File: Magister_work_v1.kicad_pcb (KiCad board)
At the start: 4 copper layers, 80 x 80 mm, 170 parts, among them J1 USB_B_Mini, J15 Conn_01x02_Pin, J17 Conn_01x04_Pin, J2 Conn_01x03_Pin, J3 Conn_01x03_Pin, J6 Conn_01x04_Pin, J7 Conn_01x02_Pin, J8 Conn_01x06_Pin, J9 Conn_01x02_Pin, Q1 AO3400A, Q10 PDTC143ET, Q11 PDTC143ET, Q12 PDTC143ET, Q2 AO3400A, Q3 PDTC143ET, Q4 PDTC143ET, Q5 PDTC143ET, Q6 PDTC143ET, Q7 PDTC143ET, Q8 PDTC143ET, Q9 PDTC143ET, SW1 SW_Push, SW10 SW_Push, SW11 SW_Push, SW12 SW_Push, SW2 SW_Push, SW3 SW_Push, SW4 SW_Push, SW5 SW_Push, SW6 SW_Push, SW7 SW_Push, SW8 SW_Push, SW9 SW_Push, U10 SRV05-4, U3 Ai-Thinker-Ra-01, U5 AMS1117-3.3, U7 STM32F407VETx, U8 AT24C256, U9 Ai-Thinker-Ra-01SH, Y1 X322525MQB4SI, Y2 SMD03215C2

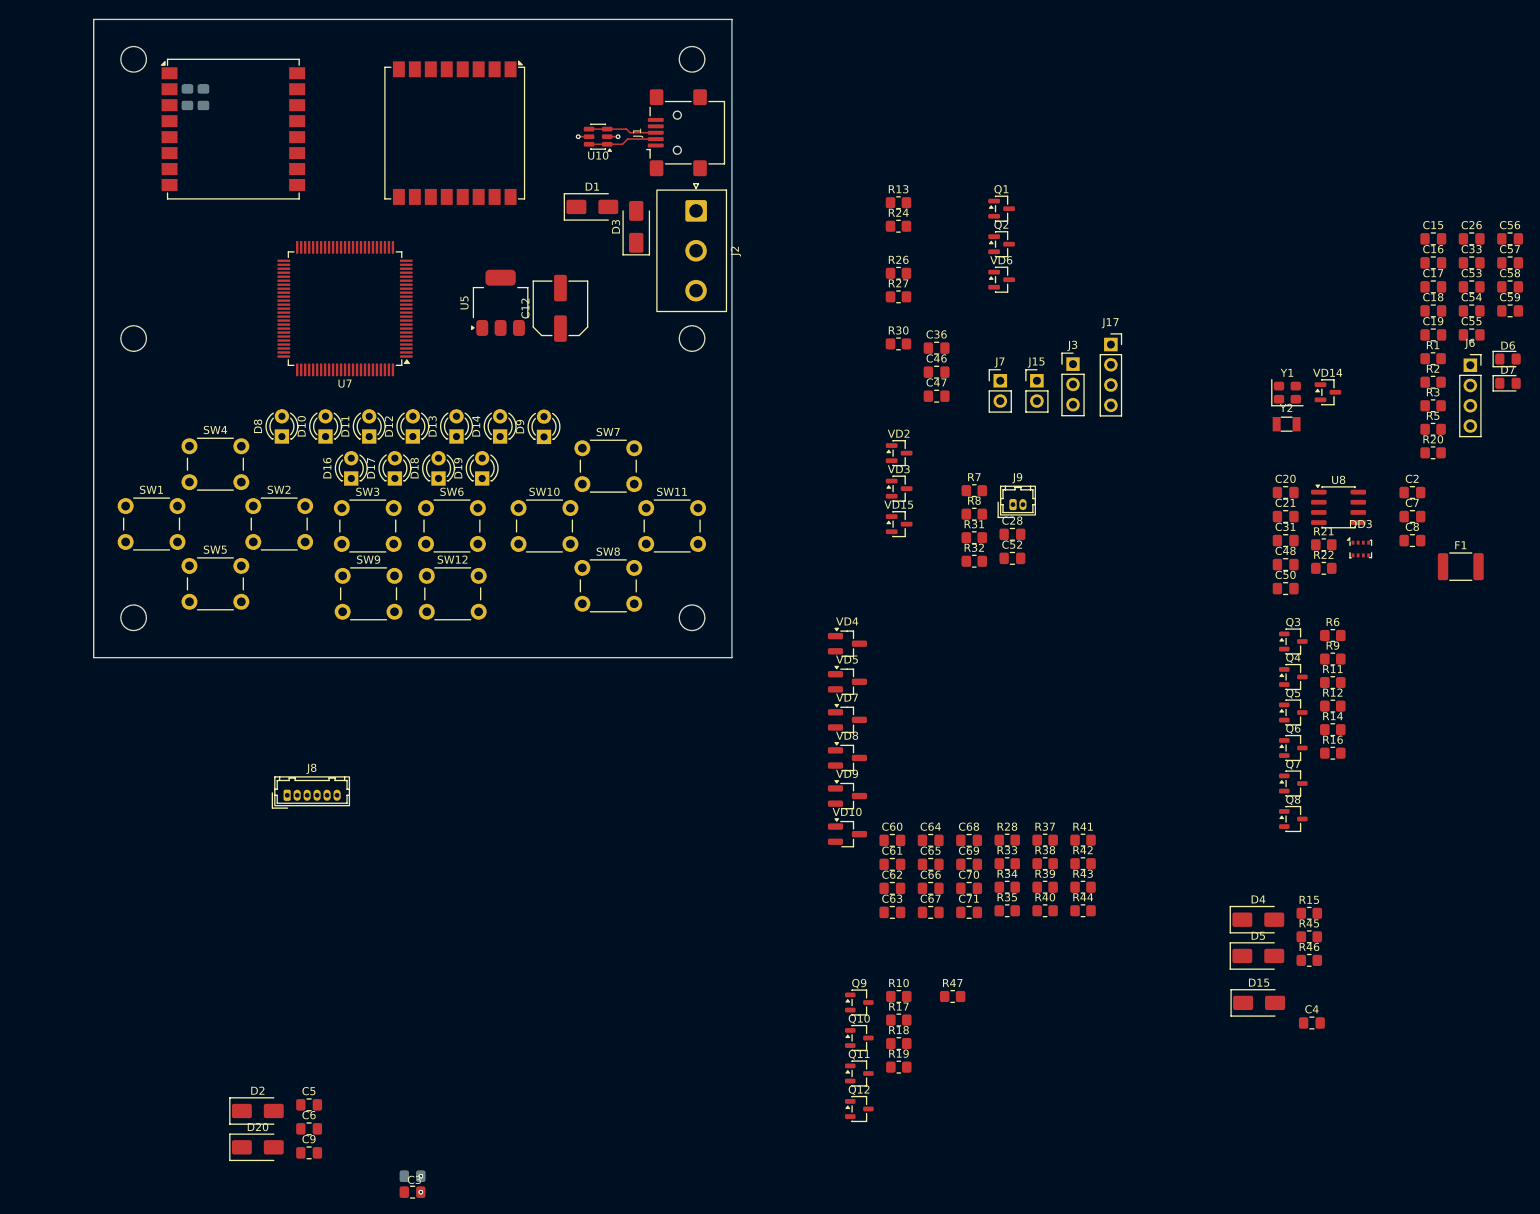
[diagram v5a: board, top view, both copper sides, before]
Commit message: feat: расположены основные узлы модуля на печатной плате
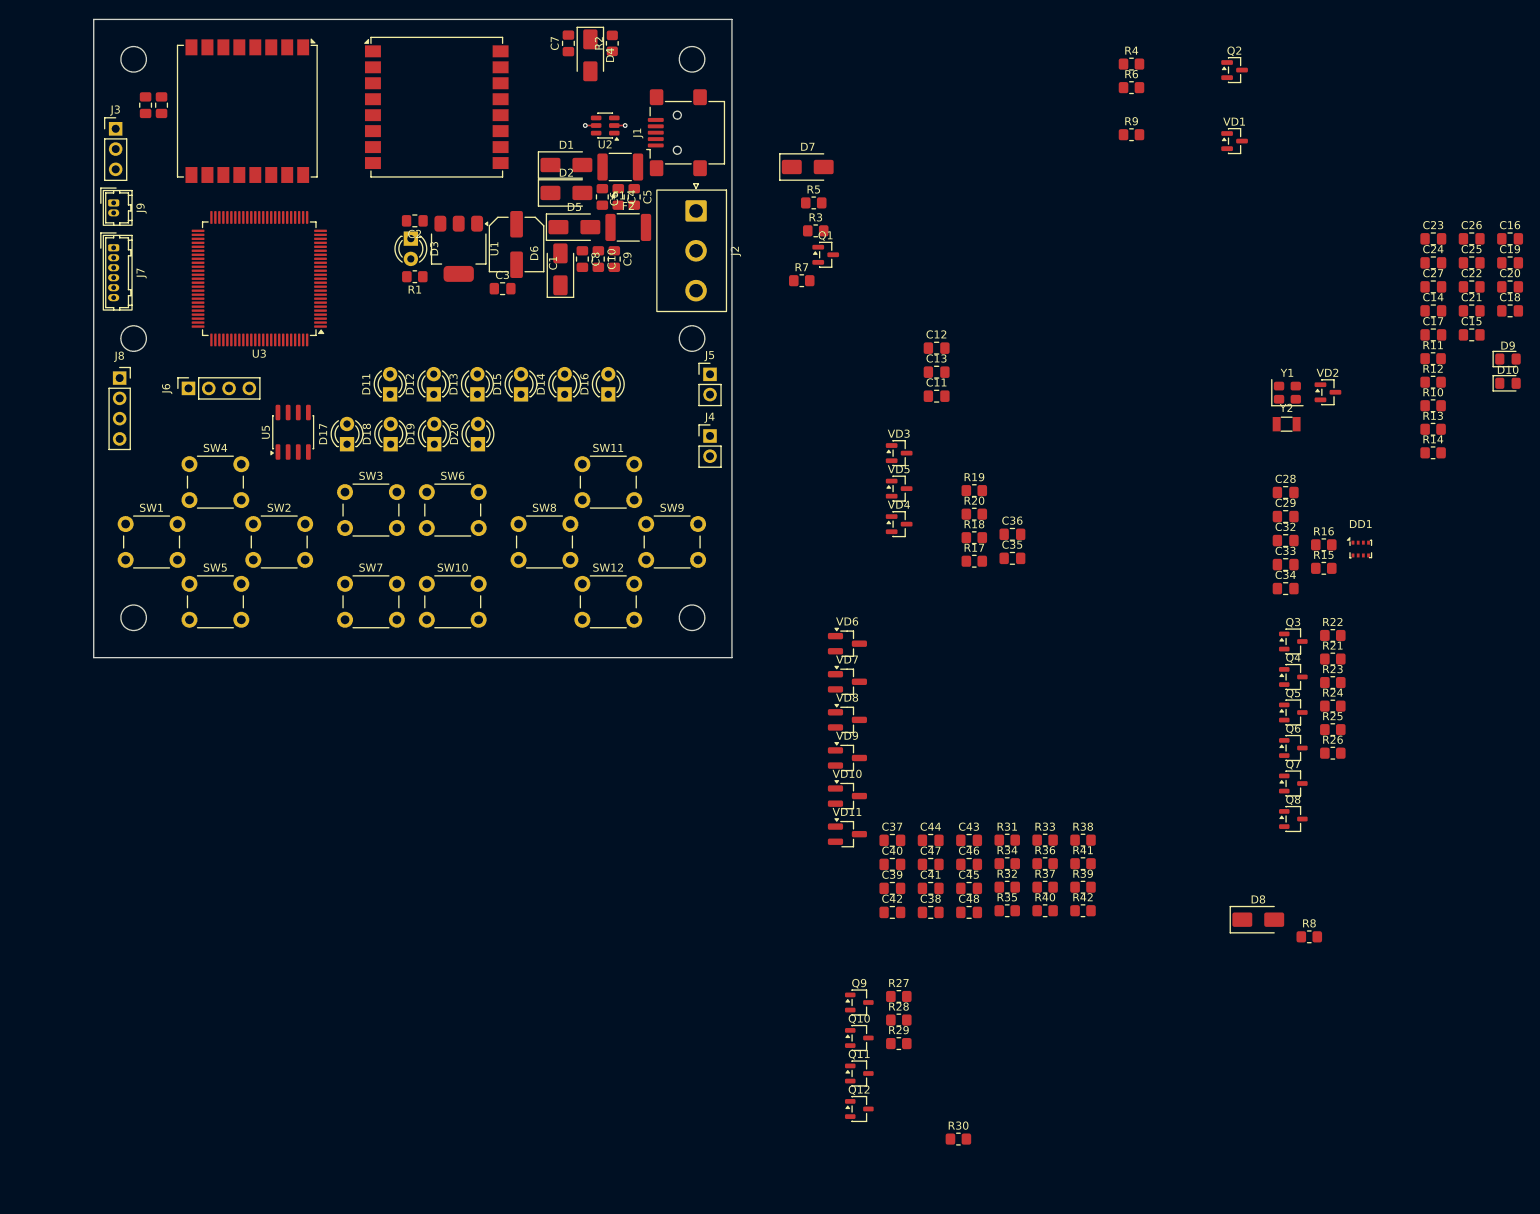
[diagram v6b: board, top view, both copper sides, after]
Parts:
- added F2: MF-MSMF110-2, Fuse:Fuse_1812_4532Metric_Pad1.30x3.40mm_HandSolder, F.Cu at (97.0, 56.1)
- C30: renamed from C32; moved to F.Cu
- C31: renamed from C49; moved to F.Cu
- C4: renamed from C1; moved to F.Cu
- moved J6 160.7 mm to (41.9, 76.2), turned to 90 degrees
- moved C7 154.2 mm to (89.5, 33.0), turned to 90 degrees
- moved D4 145.4 mm to (92.2, 34.5), turned to -90 degrees
- moved R2 139.7 mm to (95.0, 33.0), turned to 90 degrees
- moved U5 131.4 mm to (55.0, 81.8), turned to 90 degrees
- moved C2 130.4 mm to (70.2, 55.2), turned to 180 degrees
- moved C6 127.0 mm to (93.8, 52.2), turned to -90 degrees
- moved C4 125.4 mm to (95.8, 52.2), turned to -90 degrees
- moved J8 124.3 mm to (33.2, 75.0)
- moved J3 123.6 mm to (32.8, 43.7)
- moved J9 118.9 mm to (32.5, 53.0), turned to -90 degrees
- moved C3 118.3 mm to (81.2, 63.8)
- moved C10 117.8 mm to (93.2, 60.0), turned to -90 degrees
- moved D5 117.7 mm to (90.2, 56.0)
- moved F1 116.7 mm to (96.0, 48.5), turned to 180 degrees
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- renumbered C12 to C1, C9 to C10, C47 to C11, C36 to C12, C46 to C13, C18 to C14, C55 to C15, C56 to C16, C19 to C17, C59 to C18, C57 to C19, C7 to C2, C58 to C20, C54 to C21, C53 to C22, C15 to C23, C16 to C24, C33 to C25, C17 to C27, C20 to C28, C21 to C29, C8 to C3, C31 to C32, C48 to C33, C50 to C34, C52 to C35, C28 to C36, C60 to C37, C67 to C38, C62 to C39, C61 to C40, C66 to C41, C63 to C42, C68 to C43, C64 to C44, C70 to C45, C69 to C46, C65 to C47, C71 to C48, C2 to C5, C3 to C6, C4 to C7, C5 to C8, C6 to C9, D7 to D10, D8 to D11, D10 to D12, D11 to D13, D13 to D14, D12 to D15, D14 to D16, D16 to D17, D17 to D18, D18 to D19, D3 to D2, D19 to D20, D9 to D3, D15 to D4, D2 to D5, D20 to D6, D5 to D7, D4 to D8, D6 to D9, DD3 to DD1, J15 to J4, J7 to J5, J8 to J7, J17 to J8, Q2 to Q1, Q1 to Q2, R47 to R1, R3 to R10, R1 to R11, R2 to R12, R5 to R13, R20 to R14, R22 to R15, R21 to R16, R32 to R17, R31 to R18, R7 to R19, R15 to R2, R8 to R20, R9 to R21, R6 to R22, R11 to R23, R12 to R24, R14 to R25, R16 to R26, R10 to R27, R17 to R28, R18 to R29, R27 to R3, R19 to R30, R28 to R31, R34 to R32, R37 to R33, R33 to R34, R38 to R36, R39 to R37, R41 to R38, R43 to R39, R13 to R4, R42 to R41, R44 to R42, R46 to R5, R24 to R6, R30 to R7, R45 to R8, R26 to R9, SW8 to SW10, SW10 to SW11, SW3 to SW2, SW5 to SW3, SW2 to SW4, SW4 to SW5, SW9 to SW8, SW11 to SW9, U5 to U1, U10 to U2, U7 to U3, U3 to U4, U8 to U5, U9 to U6, VD6 to VD1, VD9 to VD10, VD10 to VD11, VD14 to VD2, VD2 to VD3, VD15 to VD4, VD3 to VD5, VD4 to VD6, VD5 to VD7, VD7 to VD8, VD8 to VD9
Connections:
- C10 pad 1: +5V_in -> Net-(D5-A)
- C8 pad 1: +5V_in -> Net-(D5-A)
- C9 pad 1: +5V_in -> Net-(D5-A)
- D5 pad 2: +5V_in -> Net-(D5-A)
- D6 pad 2: +5V_in -> Net-(D5-A)
- J2 pad 1: +5V_in -> Net-(F2-A1)
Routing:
- net D-: track 8.63 -> 0.00 mm
- net D+: track 8.55 -> 0.00 mm
- net GND: vias 3 -> 1

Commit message: feat: добавлена микросхема для коммутации светодиодов
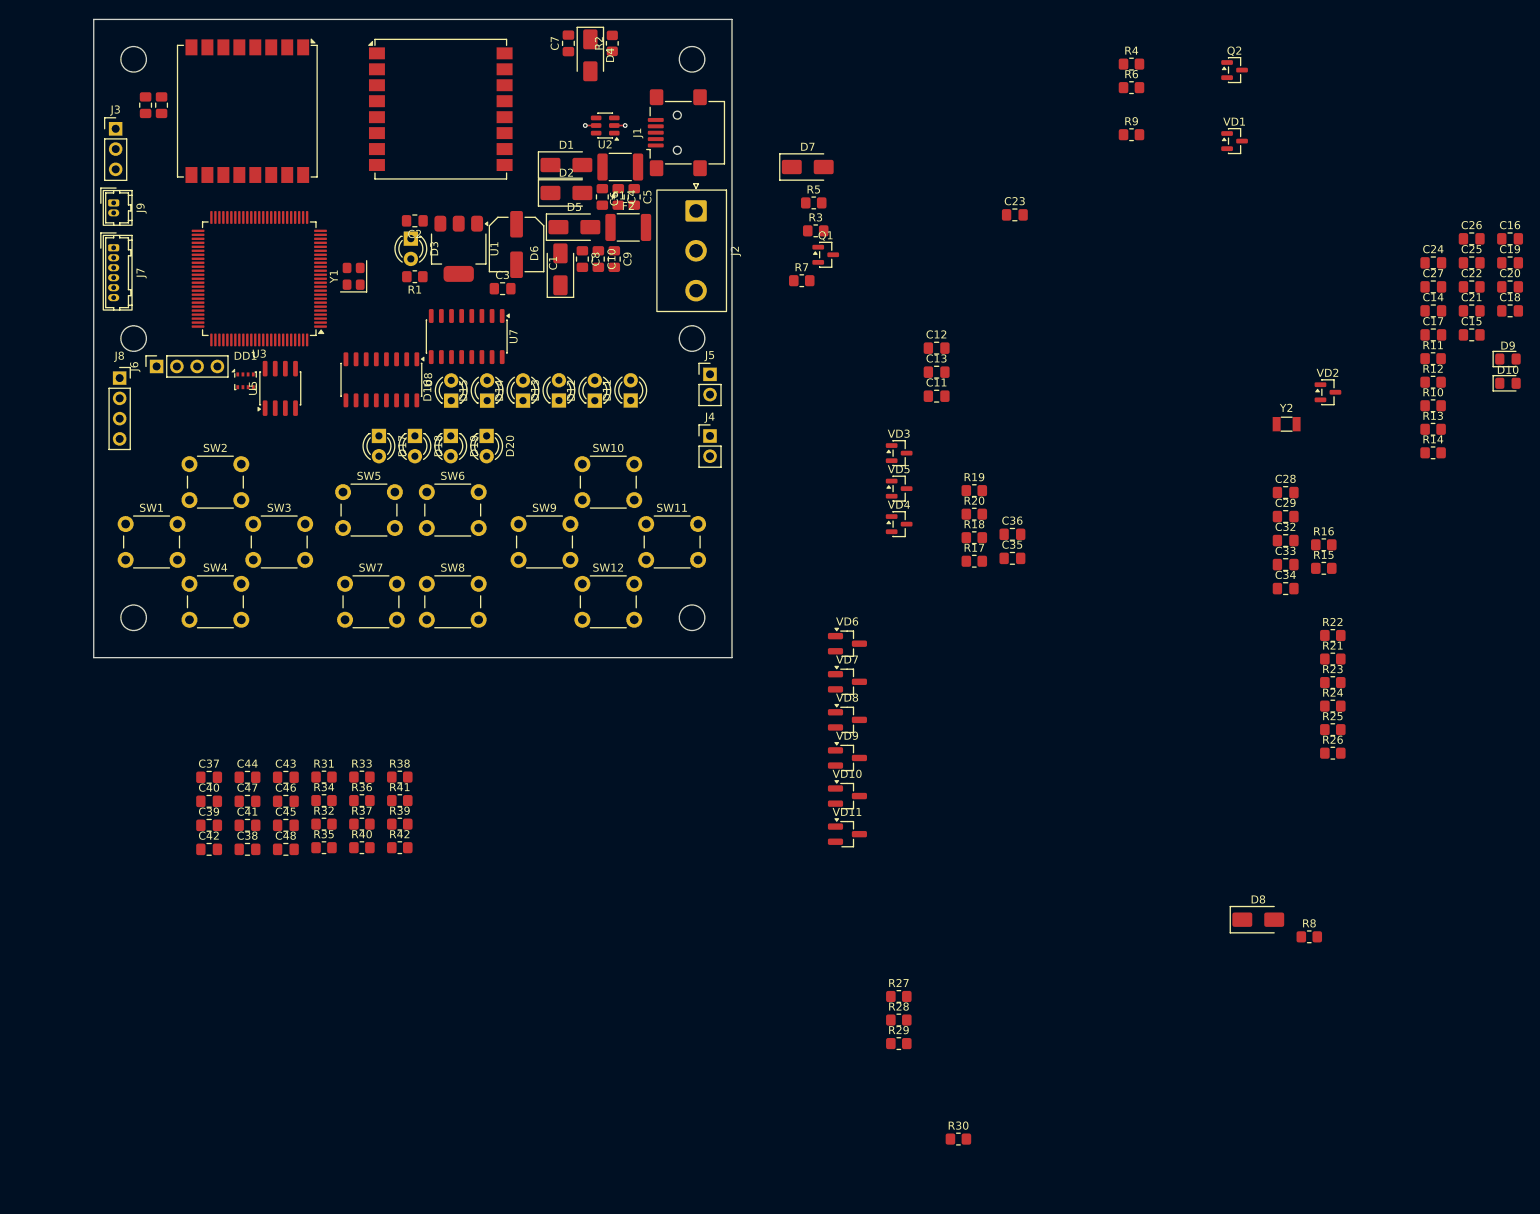
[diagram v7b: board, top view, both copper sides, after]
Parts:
- removed Q10, Q11, Q12, Q3, Q4, Q5, Q6, Q7, Q8, Q9: PDTC143ET, Package_TO_SOT_SMD:SOT-23-3
- added U7: ULN2003, Package_SO:SO-16_3.9x9.9mm_P1.27mm, F.Cu at (76.8, 69.8)
- added U8: ULN2003, Package_SO:SO-16_3.9x9.9mm_P1.27mm, F.Cu at (66.1, 75.2)
- moved DD1 141.4 mm to (49.0, 75.3)
- moved Y1 118.0 mm to (62.6, 62.2), turned to 90 degrees
- moved R31 86.0 mm to (58.9, 125.0)
- moved R32 86.0 mm to (58.9, 130.9)
- moved R33 86.0 mm to (63.6, 125.0)
- moved R34 86.0 mm to (58.9, 127.9)
- moved R35 86.0 mm to (58.9, 133.8)
- moved R36 86.0 mm to (63.6, 127.9)
- moved R37 86.0 mm to (63.6, 130.9)
- moved R38 86.0 mm to (68.4, 125.0)
- moved R39 86.0 mm to (68.4, 130.9)
- moved R40 86.0 mm to (63.6, 133.8)
- moved R41 86.0 mm to (68.4, 127.9)
- moved R42 86.0 mm to (68.4, 133.8)
- moved C37 86.0 mm to (44.5, 125.0)
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
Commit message: feat: добавлены соединения светодиодов и защитных диодов и кнопок
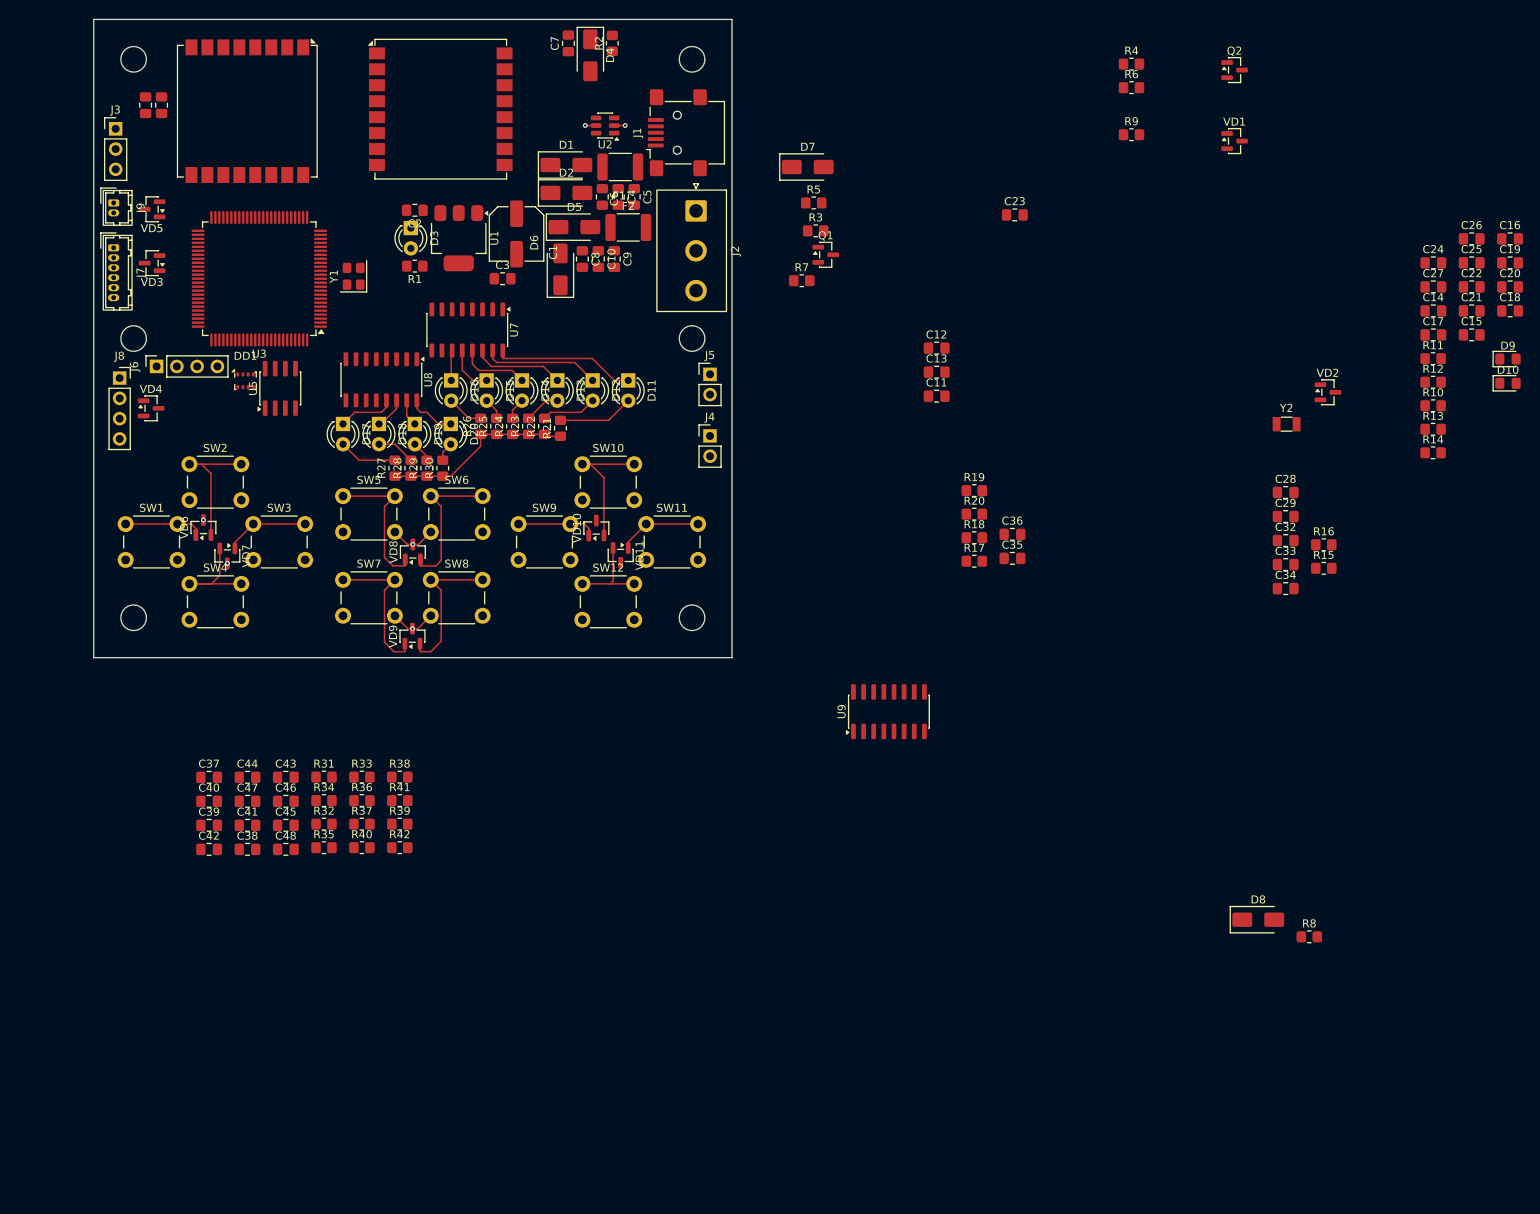
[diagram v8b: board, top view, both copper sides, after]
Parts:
- added U9: 74HC165, Package_SO:SOIC-16_3.9x9.9mm_P1.27mm, F.Cu at (129.7, 116.8)
- VD10, VD11, VD6, VD7, VD8, VD9: footprint Package_TO_SOT_SMD:SOT-23_Handsoldering -> Package_TO_SOT_SMD:SOT-23
- moved R26 114.4 mm to (78.5, 81.0), turned to 90 degrees
- moved R25 111.5 mm to (80.5, 81.0), turned to 90 degrees
- moved R24 108.6 mm to (82.5, 81.0), turned to 90 degrees
- moved R30 106.1 mm to (73.8, 86.2), turned to 90 degrees
- moved R23 105.8 mm to (84.5, 81.0), turned to 90 degrees
- moved R22 102.2 mm to (86.5, 81.0), turned to 90 degrees
- moved R21 101.0 mm to (88.5, 81.2), turned to 90 degrees
- moved VD5 100.0 mm to (37.3, 53.8), turned to 180 degrees
- moved VD3 96.6 mm to (37.3, 60.5), turned to 180 degrees
- moved VD4 94.9 mm to (37.2, 78.8)
- moved R29 93.3 mm to (71.8, 86.2), turned to 90 degrees
- moved R28 92.3 mm to (69.8, 86.2), turned to 90 degrees
- moved R27 91.5 mm to (67.8, 86.2), turned to 90 degrees
- moved VD6 82.0 mm to (43.8, 93.7), turned to 90 degrees
- moved VD7 79.3 mm to (46.8, 97.2), turned to -90 degrees
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- renumbered SW11 to SW10, SW9 to SW11, SW4 to SW2, SW2 to SW3, SW5 to SW4, SW3 to SW5, SW10 to SW8, SW8 to SW9
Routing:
- net +5V: track 1.36 -> 25.3 mm
- net Net-(VD9-K1): track 0.00 -> 18.9 mm
- net Net-(VD9-K2): track 0.00 -> 18.9 mm
- net Net-(VD8-K2): track 0.00 -> 18.8 mm
- net Net-(VD8-K1): track 0.00 -> 18.6 mm
- net Net-(D11-K): track 0.00 -> 17.9 mm
- net Net-(VD10-K2): track 0.00 -> 17.1 mm
- net Net-(VD6-K2): track 0.00 -> 15.9 mm
- net Net-(D12-K): track 0.00 -> 14.7 mm
- net Net-(VD7-K2): track 0.00 -> 14.1 mm
- net GND: track 1.36 -> 13.0 mm, vias 1 -> 5
- net Net-(D13-K): track 0.00 -> 11.4 mm
- net Net-(VD11-K2): track 0.00 -> 11.1 mm
- net Net-(VD7-K1): track 0.00 -> 10.5 mm
- net Net-(VD11-K1): track 0.00 -> 10.4 mm
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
